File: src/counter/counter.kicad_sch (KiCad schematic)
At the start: 4 parts, among them U1 74LS175, U2 74LS00, U3 74LS20, U4 74LS86

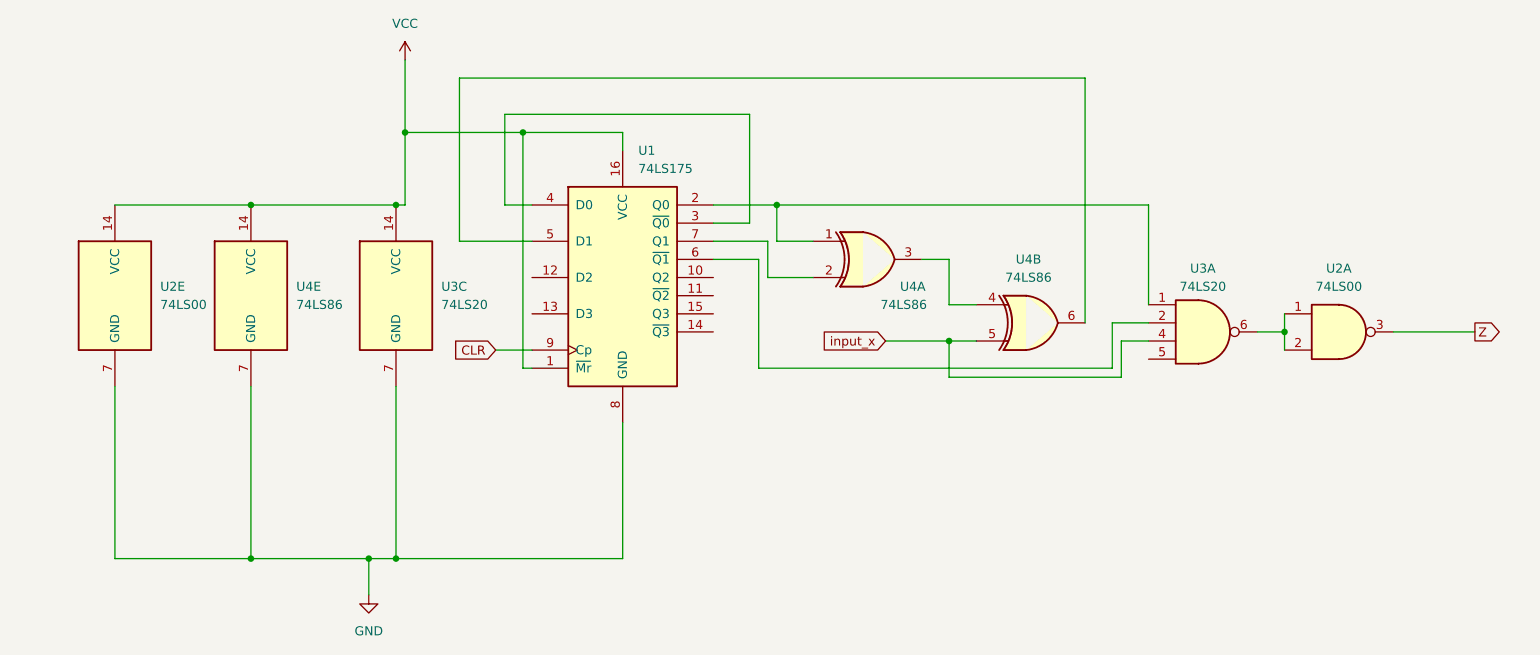
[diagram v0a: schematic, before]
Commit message: fix counter.kicad_sch counter.py
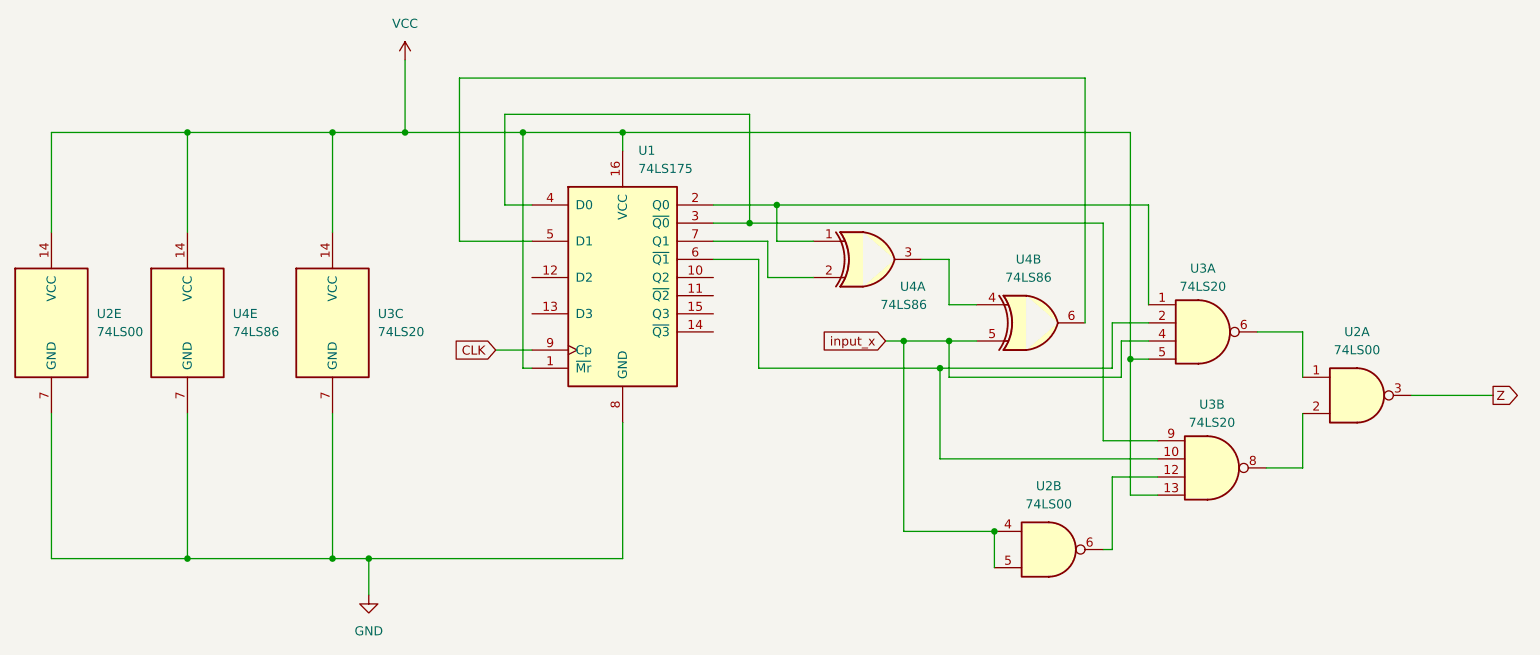
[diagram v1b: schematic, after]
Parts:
- added unit 2 of U2
- added unit 2 of U3
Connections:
- net VCC: now also U3.5, U3.13
- net input_x: now also U2.4, U2.5
- net at U1.3 (~{Q0}), U1.4 (D0): now also U3.9
- net at U1.6 (~{Q1}), U3.2: now also U3.10
- net at U2.1, U3.6: no longer U2.2
- net CLR renamed CLK
- new net: U2.6, U3.12
- new net: U2.2, U3.8
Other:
- moved on the sheet: U4E
